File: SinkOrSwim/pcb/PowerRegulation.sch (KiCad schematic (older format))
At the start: 6 parts

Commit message: First annotation
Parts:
- gave numbers to parts that had none: 6
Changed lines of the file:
@@
 $EndDescr
 $Comp
-L GND #PWR?
+L GND #PWR401
 U 1 1 54DC5473
 P 4800 3100
-F 0 "#PWR?" H 4800 2850 60  0001 C CNN
+F 0 "#PWR401" H 4800 2850 60  0001 C CNN
 F 1 "GND" H 4800 2950 60  0000 C CNN
 F 2 "" H 4800 3100 60  0000 C CNN
@@
 $EndComp
 $Comp
-L C C?
+L C C401
 U 1 1 54DC5479
 P 4150 2450
-F 0 "C?" H 4200 2550 50  0000 L CNN
+F 0 "C401" H 4200 2550 50  0000 L CNN
 F 1 "C" H 4200 2350 50  0000 L CNN
 F 2 "" H 4188 2300 30  0000 C CNN
@@
 $EndComp
 $Comp
-L C C?
+L C C402
 U 1 1 54DC5480
 P 6350 2500
-F 0 "C?" H 6400 2600 50  0000 L CNN
+F 0 "C402" H 6400 2600 50  0000 L CNN
 F 1 "C" H 6400 2400 50  0000 L CNN
 F 2 "" H 6388 2350 30  0000 C CNN
@@
 $EndComp
 $Comp
-L LM2931D-R U?
+L LM2931D-R U401
 U 1 1 54DC5489
 P 4800 2200
-F 0 "U?" H 5150 1850 40  0000 C CNN
+F 0 "U401" H 5150 1850 40  0000 C CNN
 F 1 "LM2931D-R" H 4800 2550 40  0000 C CNN
 F 2 "SO-8" H 4800 2450 35  0000 C CIN
@@
 Connection ~ 6350 2000
 $Comp
-L R R?
+L R R402
 U 1 1 54DC54AD
 P 5800 2250
-F 0 "R?" V 5880 2250 50  0000 C CNN
+F 0 "R402" V 5880 2250 50  0000 C CNN
 F 1 "27K" V 5807 2251 50  0000 C CNN
 F 2 "" V 5730 2250 30  0000 C CNN
@@
 $EndComp
 $Comp
-L R R?
+L R R403
 U 1 1 54DC54B4
 P 5800 2550
-F 0 "R?" V 5880 2550 50  0000 C CNN
+F 0 "R403" V 5880 2550 50  0000 C CNN
 F 1 "21.6K" V 5807 2551 50  0000 C CNN
 F 2 "" V 5730 2550 30  0000 C CNN
@@
 	6350 2700 6350 3000
 $Comp
-L R R?
+L R R401
 U 1 1 54DC54C6
 P 4350 2600
-F 0 "R?" V 4430 2600 50  0000 C CNN
+F 0 "R401" V 4430 2600 50  0000 C CNN
 F 1 "R" V 4357 2601 50  0000 C CNN
 F 2 "" V 4280 2600 30  0000 C CNN

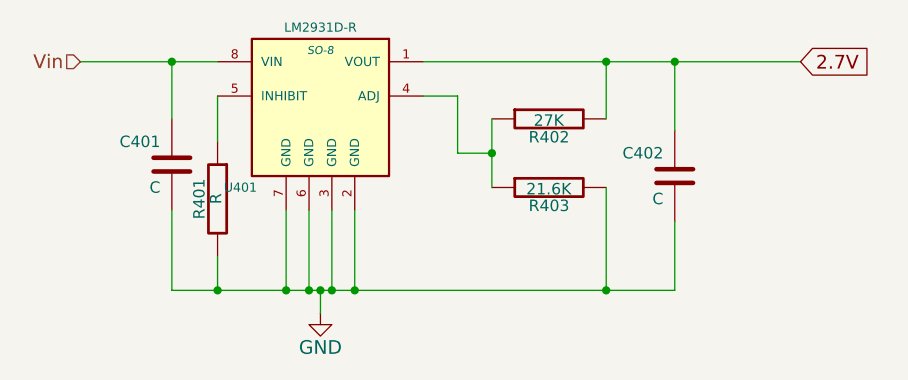
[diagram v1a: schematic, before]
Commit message: Footprints associated and parts on pcb
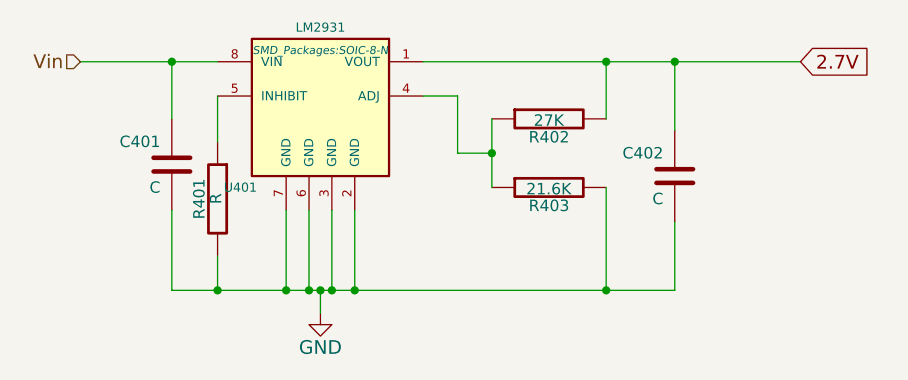
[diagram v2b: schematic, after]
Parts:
- C401, C402: footprint (none) -> Capacitors_SMD:C_0805_HandSoldering
- R401, R402, R403: footprint (none) -> Resistors_SMD:R_0805_HandSoldering
- U401: value LM2931D-R -> LM2931; footprint SO-8 -> SMD_Packages:SOIC-8-N; MPN 497-7817-1-ND -> LMD2931D-R
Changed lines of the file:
@@
 $EndDescr
 $Comp
-L GND #PWR401
+L GND #PWR07
 U 1 1 54DC5473
 P 4800 3100
-F 0 "#PWR401" H 4800 2850 60  0001 C CNN
+F 0 "#PWR07" H 4800 2850 60  0001 C CNN
 F 1 "GND" H 4800 2950 60  0000 C CNN
 F 2 "" H 4800 3100 60  0000 C CNN
@@
 F 0 "C401" H 4200 2550 50  0000 L CNN
 F 1 "C" H 4200 2350 50  0000 L CNN
-F 2 "" H 4188 2300 30  0000 C CNN
+F 2 "Capacitors_SMD:C_0805_HandSoldering" H 4188 2300 30  0001 C CNN
 F 3 "" H 4150 2450 60  0000 C CNN
 	1    4150 2450
@@
 F 0 "C402" H 6400 2600 50  0000 L CNN
 F 1 "C" H 6400 2400 50  0000 L CNN
-F 2 "" H 6388 2350 30  0000 C CNN
+F 2 "Capacitors_SMD:C_0805_HandSoldering" H 6388 2350 30  0001 C CNN
 F 3 "" H 6350 2500 60  0000 C CNN
 	1    6350 2500
@@
 P 4800 2200
 F 0 "U401" H 5150 1850 40  0000 C CNN
-F 1 "LM2931D-R" H 4800 2550 40  0000 C CNN
-F 2 "SO-8" H 4800 2450 35  0000 C CIN
-F 3 "" H 4800 2350 60  0000 C CNN
-F 4 "497-7817-1-ND" H 4800 2200 60  0001 C CNN "MPN"
+F 1 "LM2931" H 4800 2550 40  0000 C CNN
+F 2 "SMD_Packages:SOIC-8-N" H 4800 2450 35  0000 C CIN
+F 3 "http://www.st.com/web/en/resource/technical/document/datasheet/CD00001885.pdf" H 4800 2350 60  0001 C CNN
+F 4 "LMD2931D-R" H 4800 2200 60  0001 C CNN "MPN"
 	1    4800 2200
 	-1   0    0    -1
 $EndComp
 Wire Wire Line
-	4350 2000 4150 2000
-Wire Wire Line
-	4150 2000 3750 2000
+	3750 2000 4350 2000
 Wire Wire Line
 	4150 2250 4150 2000
@@
 	4800 3000 4800 3100
 Wire Wire Line
-	6900 2000 6350 2000
+	5250 2000 6900 2000
 Wire Wire Line
-	6350 2000 6050 2000
-Wire Wire Line
-	6050 2000 5250 2000
-Wire Wire Line
-	6350 3000 6050 3000
-Wire Wire Line
-	6050 3000 4950 3000
-Wire Wire Line
-	4950 3000 4850 3000
-Wire Wire Line
-	4850 3000 4800 3000
-Wire Wire Line
-	4800 3000 4750 3000
-Wire Wire Line
-	4750 3000 4650 3000
-Wire Wire Line
-	4650 3000 4350 3000
-Wire Wire Line
-	4350 3000 4150 3000
+	4150 3000 6350 3000
 Wire Wire Line
 	4150 3000 4150 2650
@@
 F 0 "R402" V 5880 2250 50  0000 C CNN
 F 1 "27K" V 5807 2251 50  0000 C CNN
-F 2 "" V 5730 2250 30  0000 C CNN
+F 2 "Resistors_SMD:R_0805_HandSoldering" V 5730 2250 30  0001 C CNN
 F 3 "" H 5800 2250 30  0000 C CNN
 	1    5800 2250
@@
 F 0 "R403" V 5880 2550 50  0000 C CNN
 F 1 "21.6K" V 5807 2551 50  0000 C CNN
-F 2 "" V 5730 2550 30  0000 C CNN
+F 2 "Resistors_SMD:R_0805_HandSoldering" V 5730 2550 30  0001 C CNN
 F 3 "" H 5800 2550 30  0000 C CNN
 	1    5800 2550
@@
 Connection ~ 6050 2000
 Wire Wire Line
-	5550 2250 5550 2400
-Wire Wire Line
-	5550 2400 5550 2550
+	5550 2250 5550 2550
 Wire Wire Line
 	6050 2550 6050 3000
@@
 Connection ~ 5550 2400
 Wire Wire Line
-	6350 2700 6350 3000
+	6350 3000 6350 2700
 $Comp
 L R R401
@@
 F 0 "R401" V 4430 2600 50  0000 C CNN
 F 1 "R" V 4357 2601 50  0000 C CNN
-F 2 "" V 4280 2600 30  0000 C CNN
+F 2 "Resistors_SMD:R_0805_HandSoldering" V 4280 2600 30  0001 C CNN
 F 3 "" H 4350 2600 30  0000 C CNN
 	1    4350 2600

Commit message: Updated Design Rules for power on pcb and redrew some traces.
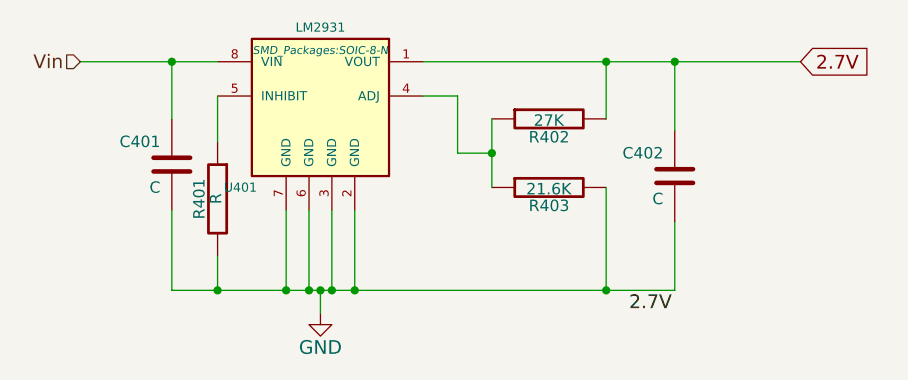
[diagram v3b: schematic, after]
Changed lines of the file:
@@
 Text HLabel 3750 2000 0    60   Input ~ 0
 Vin
+Text Label 6150 3100 0    60   ~ 0
+2.7V
 $EndSCHEMATC

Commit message: Gerbers added, BOM written
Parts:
- C401, C402: value C -> .1uf; MPN (none) -> 08055C104JAT2A
- R401: value R -> 0; MPN (none) -> CRCW08050000Z0EAHP
- R402: MPN (none) -> RMCF0805FT27K0
- R403: MPN (none) -> RMCF0805FT21K5
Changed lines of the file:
@@
 P 4150 2450
 F 0 "C401" H 4200 2550 50  0000 L CNN
-F 1 "C" H 4200 2350 50  0000 L CNN
+F 1 ".1uf" H 4200 2350 50  0000 L CNN
 F 2 "Capacitors_SMD:C_0805_HandSoldering" H 4188 2300 30  0001 C CNN
-F 3 "" H 4150 2450 60  0000 C CNN
+F 3 "http://www.avx.com/docs/Catalogs/cx7r.pdf" H 4150 2450 60  0001 C CNN
+F 4 "08055C104JAT2A" H 4150 2450 60  0001 C CNN "MPN"
 	1    4150 2450
 	-1   0    0    -1
@@
 P 6350 2500
 F 0 "C402" H 6400 2600 50  0000 L CNN
-F 1 "C" H 6400 2400 50  0000 L CNN
+F 1 ".1uf" H 6400 2400 50  0000 L CNN
 F 2 "Capacitors_SMD:C_0805_HandSoldering" H 6388 2350 30  0001 C CNN
-F 3 "" H 6350 2500 60  0000 C CNN
+F 3 "http://www.avx.com/docs/Catalogs/cx7r.pdf" H 6350 2500 60  0001 C CNN
+F 4 "08055C104JAT2A" H 6350 2500 60  0001 C CNN "MPN"
 	1    6350 2500
 	-1   0    0    -1
@@
 F 1 "27K" V 5807 2251 50  0000 C CNN
 F 2 "Resistors_SMD:R_0805_HandSoldering" V 5730 2250 30  0001 C CNN
-F 3 "" H 5800 2250 30  0000 C CNN
+F 3 "http://www.seielect.com/Catalog/SEI-RMCF_RMCP.pdf" H 5800 2250 30  0001 C CNN
+F 4 "RMCF0805FT27K0" H 5800 2250 60  0001 C CNN "MPN"
 	1    5800 2250
 	0    -1   1    0
@@
 F 1 "21.6K" V 5807 2551 50  0000 C CNN
 F 2 "Resistors_SMD:R_0805_HandSoldering" V 5730 2550 30  0001 C CNN
-F 3 "" H 5800 2550 30  0000 C CNN
+F 3 "http://www.seielect.com/Catalog/SEI-RMCF_RMCP.pdf" H 5800 2550 30  0001 C CNN
+F 4 "RMCF0805FT21K5" H 5800 2550 60  0001 C CNN "MPN"
 	1    5800 2550
 	0    -1   1    0
@@
 P 4350 2600
 F 0 "R401" V 4430 2600 50  0000 C CNN
-F 1 "R" V 4357 2601 50  0000 C CNN
+F 1 "0" V 4357 2601 50  0000 C CNN
 F 2 "Resistors_SMD:R_0805_HandSoldering" V 4280 2600 30  0001 C CNN
-F 3 "" H 4350 2600 30  0000 C CNN
+F 3 "http://www.vishay.com/docs/20043/crcwhpe3.pdf" H 4350 2600 30  0001 C CNN
+F 4 "CRCW08050000Z0EAHP" H 4350 2600 60  0001 C CNN "MPN"
 	1    4350 2600
 	-1   0    0    -1
